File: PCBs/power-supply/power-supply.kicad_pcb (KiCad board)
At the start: 2 copper layers, 102.9 x 81.3 mm, 13 parts, among them U3 TL783

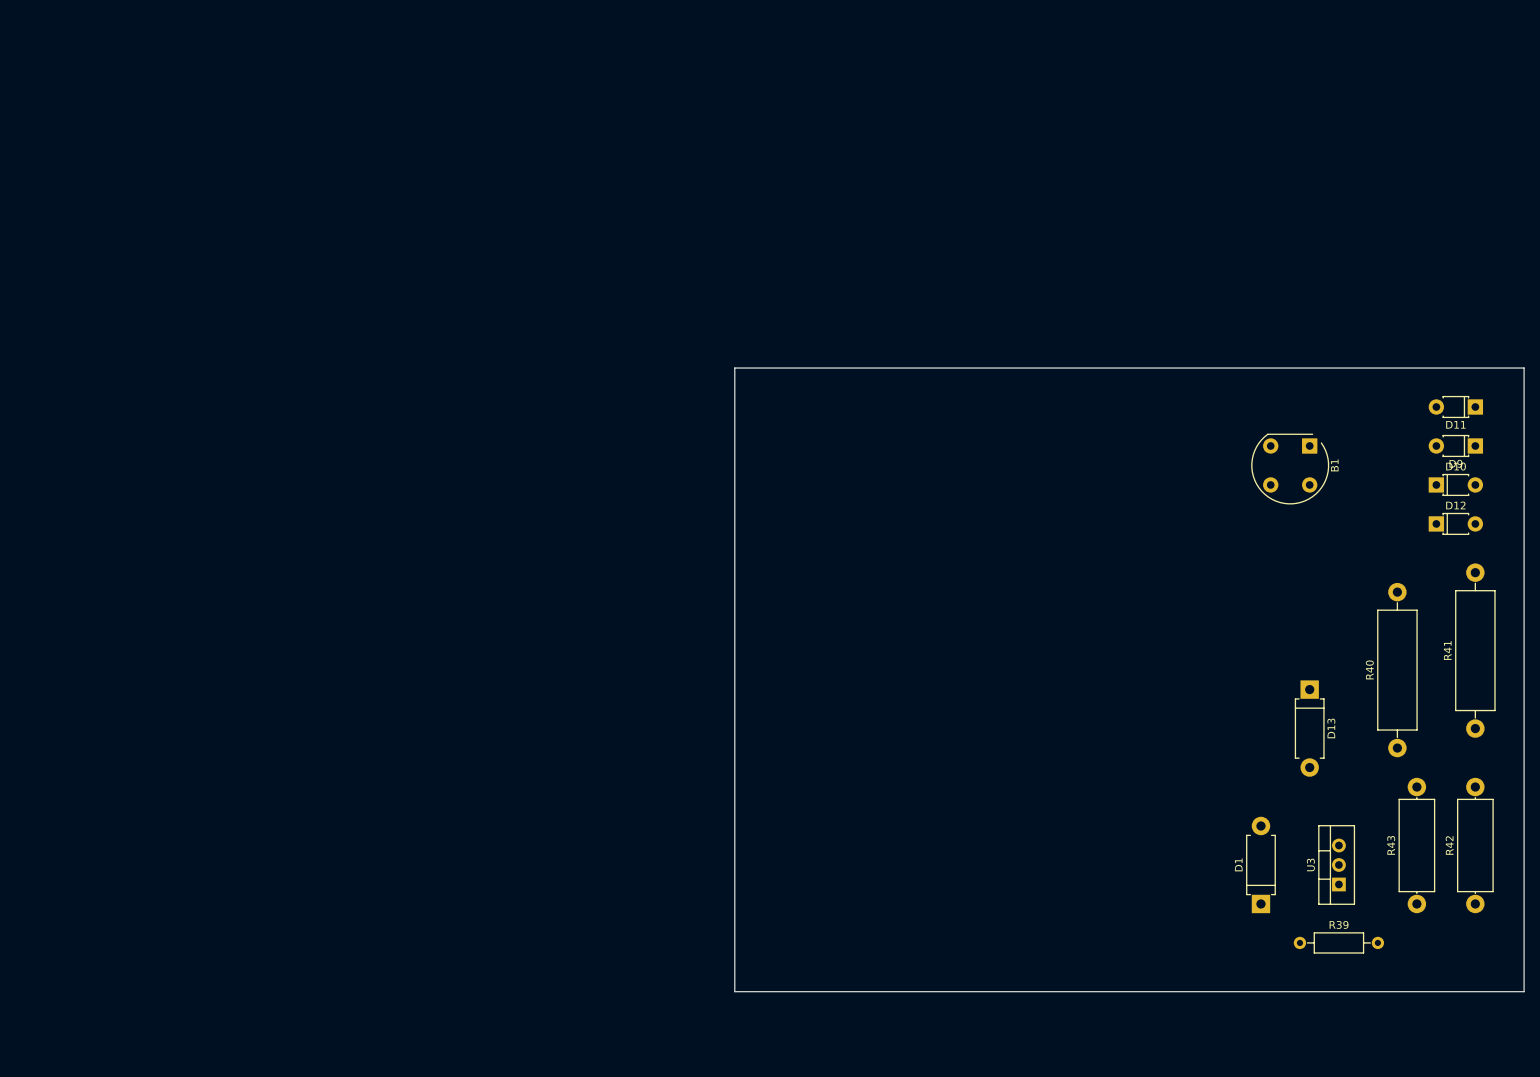
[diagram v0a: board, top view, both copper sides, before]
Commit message: First kicad version of power supply .
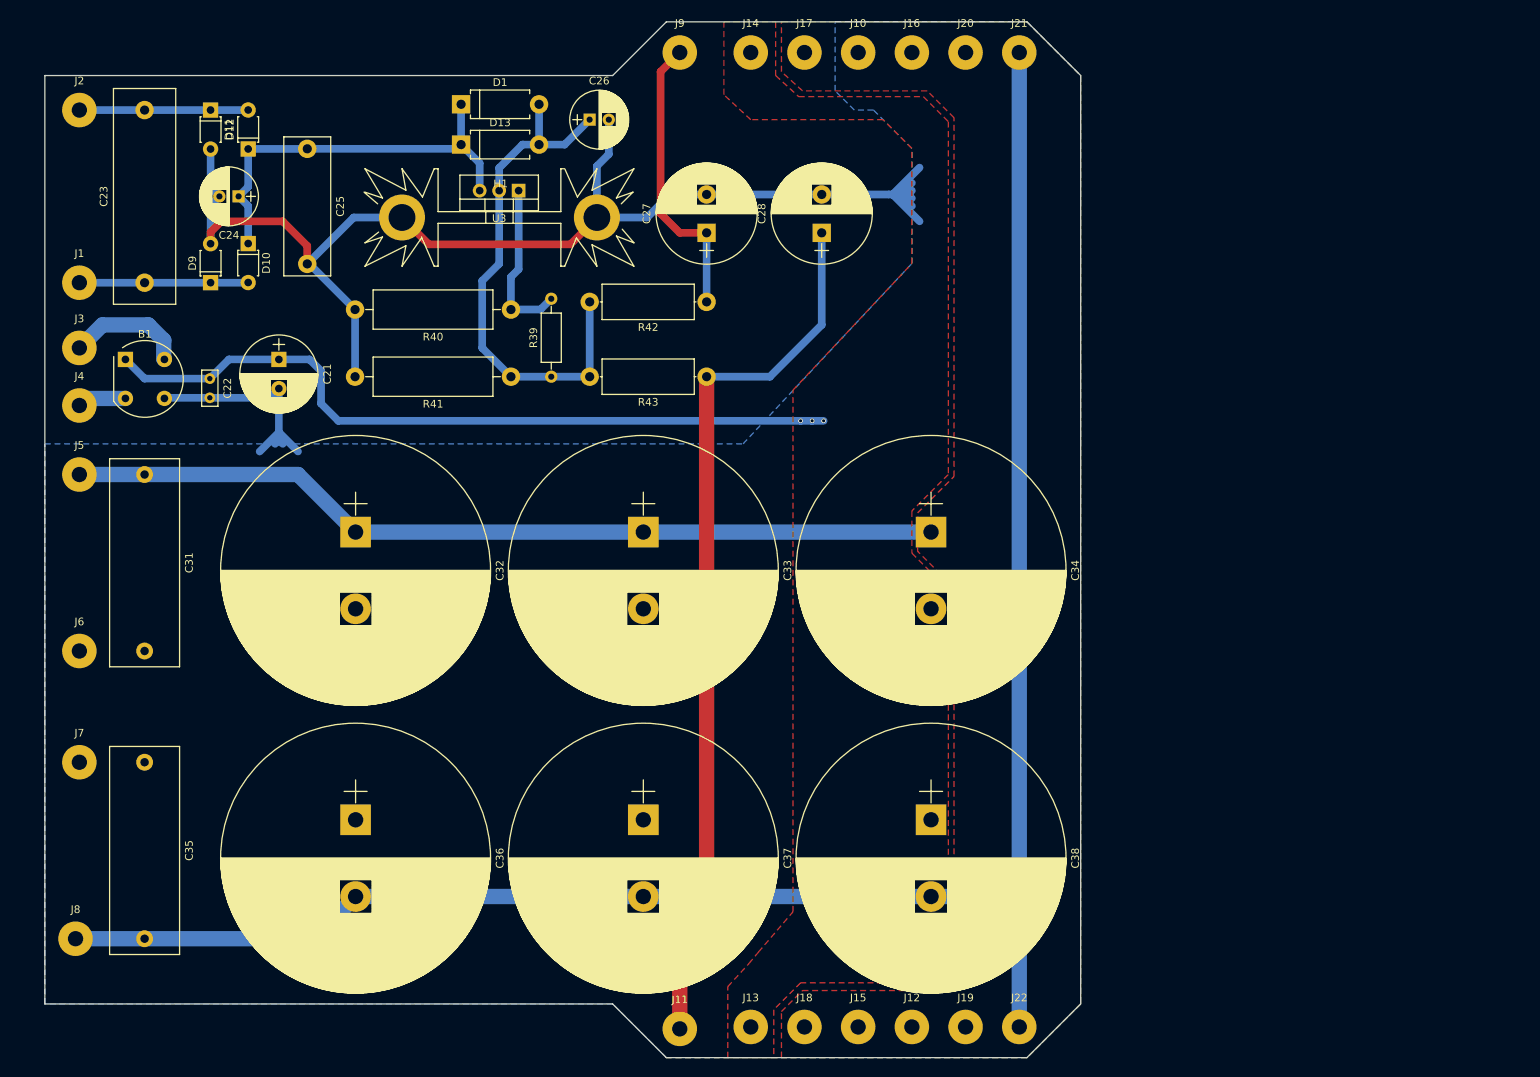
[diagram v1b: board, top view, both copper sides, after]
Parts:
- added C21: 220u, Capacitors_THT:CP_Radial_D10.0mm_P3.80mm, F.Cu at (62.5, 70.0)
- added C22: 100n, Capacitors_THT:C_Rect_L4.6mm_W2.0mm_P2.50mm_MKS02_FKP02, F.Cu at (53.5, 72.5)
- added C23: 2n2, Capacitors_THT:C_Rect_L28.0mm_W8.0mm_P22.50mm_MKS4, F.Cu at (45.0, 60.0)
- added C24: 150u, Capacitors_THT:CP_Radial_D7.5mm_P2.50mm, F.Cu at (57.2, 48.8)
- added C25: 100n, Capacitors_THT:C_Rect_L18.0mm_W6.0mm_P15.00mm_FKS3_FKP3, F.Cu at (66.2, 42.5)
- added C26: 10u, Capacitors_THT:CP_Radial_D7.5mm_P2.50mm, F.Cu at (103.0, 38.8)
- added C27: 22u, Capacitors_THT:CP_Radial_D13.0mm_P5.00mm, F.Cu at (118.2, 53.5)
- added C28: 22u, Capacitors_THT:CP_Radial_D13.0mm_P5.00mm, F.Cu at (133.2, 53.5)
- added C31: 2n2, Capacitors_THT:C_Rect_L27.0mm_W9.0mm_P23.00mm, F.Cu at (45.0, 85.0)
- added C32: 4700u, Capacitors_THT:CP_Radial_D35.0mm_P10.00mm_SnapIn, F.Cu at (72.5, 92.5)
- added C33: 4700u, Capacitors_THT:CP_Radial_D35.0mm_P10.00mm_SnapIn, F.Cu at (110.0, 92.5)
- added C34: 4700u, Capacitors_THT:CP_Radial_D35.0mm_P10.00mm_SnapIn, F.Cu at (147.5, 92.5)
- added C35: 2n2, Capacitors_THT:C_Rect_L27.0mm_W9.0mm_P23.00mm, F.Cu at (45.0, 122.5)
- added C36: 4700u, Capacitors_THT:CP_Radial_D35.0mm_P10.00mm_SnapIn, F.Cu at (72.5, 130.0)
- added C37: 4700u, Capacitors_THT:CP_Radial_D35.0mm_P10.00mm_SnapIn, F.Cu at (110.0, 130.0)
- added C38: 4700u, Capacitors_THT:CP_Radial_D35.0mm_P10.00mm_SnapIn, F.Cu at (147.5, 130.0)
- added H1: Heatsink, Heatsinks:Heatsink_Fischer_SK104-STCB_35x13mm__2xDrill3.5mm_ScrewM3, F.Cu at (91.2, 51.5)
- added J1: 250V-A, Wire_Pads:SolderWirePad_single_2mmDrill, F.Cu at (36.5, 60.0)
- added J10: 0V, Wire_Pads:SolderWirePad_single_2mmDrill, F.Cu at (138.0, 30.0)
- added J11: +310V-L, Wire_Pads:SolderWirePad_single_2mmDrill, F.Cu at (114.8, 157.2)
- added J12: 0V, Wire_Pads:SolderWirePad_single_2mmDrill, F.Cu at (145.0, 157.0)
- added J13: +42V, Wire_Pads:SolderWirePad_single_2mmDrill, F.Cu at (124.0, 157.0)
- added J14: +42V, Wire_Pads:SolderWirePad_single_2mmDrill, F.Cu at (124.0, 30.0)
- added J15: 0V, Wire_Pads:SolderWirePad_single_2mmDrill, F.Cu at (138.0, 157.0)
- added J16: 0V, Wire_Pads:SolderWirePad_single_2mmDrill, F.Cu at (145.0, 30.0)
- added J17: +38V, Wire_Pads:SolderWirePad_single_2mmDrill, F.Cu at (131.0, 30.0)
- added J18: +38V, Wire_Pads:SolderWirePad_single_2mmDrill, F.Cu at (131.0, 157.0)
- added J19: 0V, Wire_Pads:SolderWirePad_single_2mmDrill, F.Cu at (152.0, 157.0)
- added J2: 250V-B, Wire_Pads:SolderWirePad_single_2mmDrill, F.Cu at (36.5, 37.5)
- added J20: 0V, Wire_Pads:SolderWirePad_single_2mmDrill, F.Cu at (152.0, 30.0)
- added J21: -38V, Wire_Pads:SolderWirePad_single_2mmDrill, F.Cu at (159.0, 30.0)
- added J22: -38V, Wire_Pads:SolderWirePad_single_2mmDrill, F.Cu at (159.0, 157.0)
- added J3: 30V-A, Wire_Pads:SolderWirePad_single_2mmDrill, F.Cu at (36.5, 68.5)
- added J4: 30V-B, Wire_Pads:SolderWirePad_single_2mmDrill, F.Cu at (36.5, 76.0)
- added J5: 28V-A, Wire_Pads:SolderWirePad_single_2mmDrill, F.Cu at (36.5, 85.0)
- added J6: 28V-B, Wire_Pads:SolderWirePad_single_2mmDrill, F.Cu at (36.5, 108.0)
- added J7: 28V-C, Wire_Pads:SolderWirePad_single_2mmDrill, F.Cu at (36.5, 122.5)
- added J8: 28V-D, Wire_Pads:SolderWirePad_single_2mmDrill, F.Cu at (36.0, 145.5)
- added J9: +310V-R, Wire_Pads:SolderWirePad_single_2mmDrill, F.Cu at (114.8, 30.0)
- moved D11 169.3 mm to (53.6, 37.5), turned to 270 degrees
- moved D9 166.2 mm to (53.6, 60.0), turned to 90 degrees
- moved D12 162.4 mm to (58.5, 42.6), turned to 90 degrees
- moved D10 158.0 mm to (58.5, 54.9), turned to 270 degrees
- moved B1 154.8 mm to (42.5, 70.0), turned to 0 degrees
- moved D1 147.4 mm to (86.2, 36.8), turned to 0 degrees
- moved U3 140.0 mm to (93.8, 48.0), turned to 180 degrees
- moved R41 133.8 mm to (92.8, 72.2), turned to 180 degrees
- moved D13 131.4 mm to (86.2, 42.0), turned to 0 degrees
- moved R40 128.9 mm to (92.8, 63.5), turned to 180 degrees
- moved R42 127.3 mm to (118.2, 62.5), turned to 180 degrees
- moved R39 122.3 mm to (98.0, 72.2), turned to 90 degrees
- moved R43 115.3 mm to (118.2, 72.2), turned to 180 degrees
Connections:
- B1 pad 3: Net-(B1-Pad3) -> GND
- D11 pad 2: Net-(D11-Pad2) -> GND
- D9 pad 2: Net-(D11-Pad2) -> GND
- R40 pad 2: Net-(D11-Pad2) -> GND
- R41 pad 2: Net-(D11-Pad2) -> GND
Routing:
- net Net-(C35-Pad2): track 0.00 -> 265.9 mm
- net GND: track 0.00 -> 193.9 mm
- net Net-(C28-Pad1): track 0.00 -> 116.2 mm
- net Net-(C31-Pad1): track 0.00 -> 114.1 mm
- net Net-(B1-Pad1): track 0.00 -> 98.9 mm, vias 0 -> 3
- net Net-(C26-Pad1): track 0.00 -> 69.3 mm
- net Net-(C24-Pad1): track 0.00 -> 53.6 mm
- net Net-(C27-Pad1): track 0.00 -> 38.1 mm
- net Net-(C23-Pad1): track 0.00 -> 22.0 mm
- net Net-(C23-Pad2): track 0.00 -> 22.0 mm
- net Net-(R39-Pad2): track 0.00 -> 21.7 mm
- net Net-(B1-Pad4): track 0.00 -> 15.6 mm
- net Net-(B1-Pad2): track 0.00 -> 6.38 mm
- added copper zone on B.Cu, net GND
- added copper zone on F.Cu, net Net-(B1-Pad1)
- added copper zone on F.Cu, net Net-(C31-Pad1)
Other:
- board size 102.9 x 81.3 mm -> 135 x 135 mm
- net class Power added: clearance 0.2, trace_width 2, via_dia 0.6, via_drill 0.4
- net class power_small added: clearance 0.2, trace_width 1, via_dia 0.6, via_drill 0.4

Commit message: Small change.
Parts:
- moved J21 126.1 mm to (33.0, 34.5), turned to 90 degrees
- moved J22 122.5 mm to (160.0, 34.5), turned to 90 degrees
- moved J2 119.6 mm to (40.5, 157.0), turned to 90 degrees
- moved J20 119.6 mm to (33.0, 41.5), turned to 90 degrees
- moved J19 115.8 mm to (160.0, 41.5), turned to 90 degrees
- moved J16 113.5 mm to (33.0, 48.5), turned to 90 degrees
- moved J8 113.1 mm to (148.5, 157.5), turned to 90 degrees
- moved J12 109.5 mm to (160.0, 48.5), turned to 90 degrees
- moved J10 108.1 mm to (33.0, 55.5), turned to 90 degrees
- moved J15 103.9 mm to (160.0, 55.5), turned to 90 degrees
- moved J17 103.2 mm to (33.0, 62.5), turned to 90 degrees
- moved D11 103.2 mm to (40.5, 139.9), turned to 0 degrees
- moved J1 100.6 mm to (63.0, 157.0), turned to 90 degrees
- moved J14 99.2 mm to (33.0, 69.5), turned to 90 degrees
- moved J18 98.8 mm to (160.0, 62.5), turned to 90 degrees
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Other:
- outline, holes or cut-outs redrawn

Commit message: Changed footprints to kicad 5 names.
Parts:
- removed H1: Heatsink, Heatsinks:Heatsink_Fischer_SK104-STCB_35x13mm__2xDrill3.5mm_ScrewM3
- added HS1: Heatsink_PAD, Heatsink:Heatsink_Fischer_SK104-STC-STIC_35x13mm_2xDrill2.5mm, F.Cu at (54.4, 102.1)
- B1: footprint Diodes_THT:Diode_Bridge_Round_D9.8mm -> Diode_THT:Diode_Bridge_Round_D9.8mm
- C21: footprint Capacitors_THT:CP_Radial_D10.0mm_P3.80mm -> Capacitor_THT:CP_Radial_D10.0mm_P3.80mm
- C22: footprint Capacitors_THT:C_Rect_L4.6mm_W2.0mm_P2.50mm_MKS02_FKP02 -> Capacitor_THT:C_Rect_L4.6mm_W2.0mm_P2.50mm_MKS02_FKP02
- C23: footprint Capacitors_THT:C_Rect_L28.0mm_W8.0mm_P22.50mm_MKS4 -> Capacitor_THT:C_Rect_L28.0mm_W8.0mm_P22.50mm_MKS4
- C24, C26: footprint Capacitors_THT:CP_Radial_D7.5mm_P2.50mm -> Capacitor_THT:CP_Radial_D7.5mm_P2.50mm
- C25: footprint Capacitors_THT:C_Rect_L18.0mm_W6.0mm_P15.00mm_FKS3_FKP3 -> Capacitor_THT:C_Rect_L18.0mm_W6.0mm_P15.00mm_FKS3_FKP3
- C27, C28: footprint Capacitors_THT:CP_Radial_D13.0mm_P5.00mm -> Capacitor_THT:CP_Radial_D13.0mm_P5.00mm
- C31, C35: footprint Capacitors_THT:C_Rect_L27.0mm_W9.0mm_P23.00mm -> Capacitor_THT:C_Rect_L27.0mm_W9.0mm_P23.00mm
- C32, C33, C34, C36, C37, C38: footprint Capacitors_THT:CP_Radial_D35.0mm_P10.00mm_SnapIn -> Capacitor_THT:CP_Radial_D35.0mm_P10.00mm_SnapIn
- D1, D13: footprint Diodes_THT:D_DO-15_P10.16mm_Horizontal -> Diode_THT:D_DO-15_P10.16mm_Horizontal
- D10, D11, D12, D9: footprint Diodes_THT:D_T-1_P5.08mm_Horizontal -> Diode_THT:D_T-1_P5.08mm_Horizontal
- J1, J10, J11, J12, J13, J14, J15, J16, J17, J18, J19, J2, J20, J21, J22, J3, J4, J5, J6, J7, J8, J9: footprint Wire_Pads:SolderWirePad_single_2mmDrill -> Connector_Wire:SolderWirePad_single_2mmDrill
- R39: footprint Resistors_THT:R_Axial_DIN0207_L6.3mm_D2.5mm_P10.16mm_Horizontal -> Resistor_THT:R_Axial_DIN0207_L6.3mm_D2.5mm_P10.16mm_Horizontal
- R40, R41: footprint Resistors_THT:R_Axial_DIN0516_L15.5mm_D5.0mm_P20.32mm_Horizontal -> Resistor_THT:R_Axial_DIN0516_L15.5mm_D5.0mm_P20.32mm_Horizontal
- R42, R43: footprint Resistors_THT:R_Axial_DIN0414_L11.9mm_D4.5mm_P15.24mm_Horizontal -> Resistor_THT:R_Axial_DIN0414_L11.9mm_D4.5mm_P15.24mm_Horizontal
- U3: footprint TO_SOT_Packages_THT:TO-220_Vertical -> Package_TO_SOT_THT:TO-220-3_Vertical
- moved U3 0.71 mm to (50.3, 99.8)
